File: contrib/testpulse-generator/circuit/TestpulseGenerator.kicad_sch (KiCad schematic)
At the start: 10 parts, among them Q1 STP16NF06, SW1 SW_DIP_x01, U1 Pico

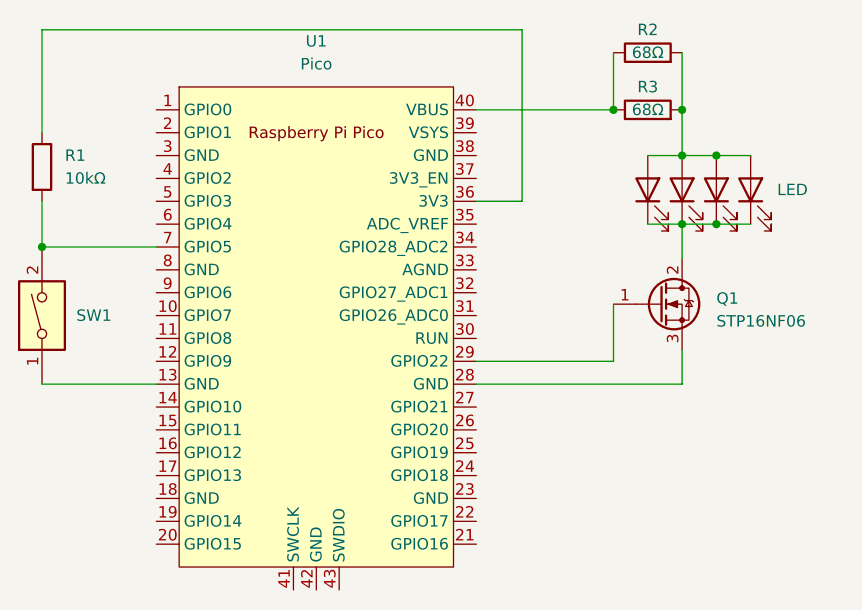
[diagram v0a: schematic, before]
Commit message: testpulse-generator: Drive TTL out separately
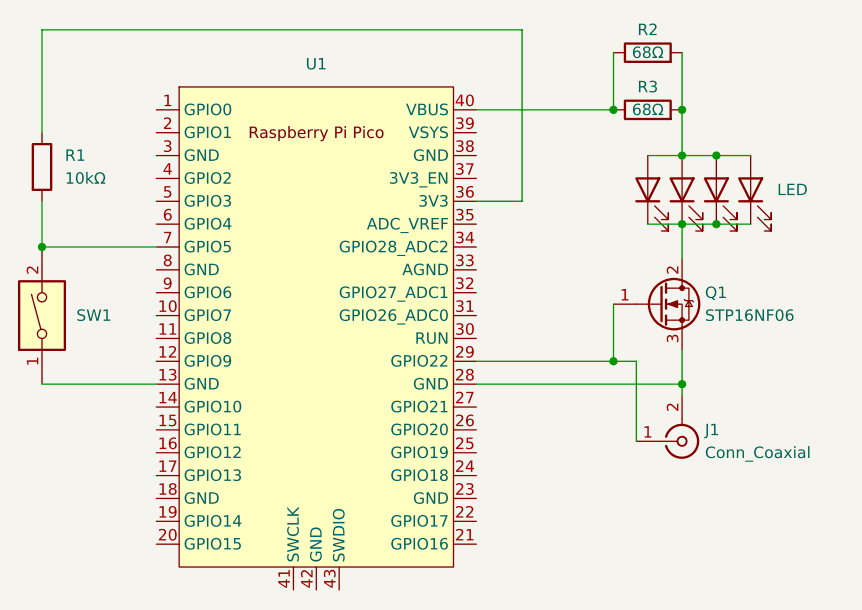
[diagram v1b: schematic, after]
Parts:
- added J1: Conn_Coaxial, symbol Connector:Conn_Coaxial
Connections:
- net at Q1.3 (S), U1.28 (GND): now also J1.2 (Ext)
- net at Q1.1 (G), U1.29 (GPIO22): now also J1.1 (In)
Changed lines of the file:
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@@
   (junction (at 106.68 52.07) (diameter 0) (color 0 0 0 0)
   )
+  (junction (at 99.06 67.31) (diameter 0) (color 0 0 0 0)
+  )
   (junction (at 99.06 39.37) (diameter 0) (color 0 0 0 0)
   )
   (junction (at 106.68 39.37) (diameter 0) (color 0 0 0 0)
   )
+  (junction (at 106.68 69.85) (diameter 0) (color 0 0 0 0)
+  )
   (junction (at 106.68 44.45) (diameter 0) (color 0 0 0 0)
   )
@@
     (stroke (width 0) (type default))
   )
+  (wire (pts (xy 101.6 67.31) (xy 99.06 67.31))
+    (stroke (width 0) (type default))
+  )
   (wire (pts (xy 110.49 44.45) (xy 114.3 44.45))
     (stroke (width 0) (type default))
@@
     (stroke (width 0) (type default))
   )
+  (wire (pts (xy 106.68 69.85) (xy 106.68 71.12))
+    (stroke (width 0) (type default))
+  )
   (wire (pts (xy 106.68 52.07) (xy 110.49 52.07))
+    (stroke (width 0) (type default))
+  )
+  (wire (pts (xy 101.6 76.2) (xy 101.6 67.31))
     (stroke (width 0) (type default))
   )
@@
   )
   (symbol (lib_id "Device:R") (at 35.56 45.72 0) (unit 1)
-    (in_bom yes) (on_board yes) (dnp no) (fields_autoplaced)
-    (property "Reference" "R1" (at 38.1 44.4499 0)
-      (effects (font (size 1.27 1.27)) (justify left))
-    )
-    (property "Value" "10kΩ" (at 38.1 46.9899 0)
+    (in_bom yes) (on_board yes) (dnp no)
+    (property "Reference" "R1" (at 38.1 44.45 0)
+      (effects (font (size 1.27 1.27)) (justify left))
+    )
+    (property "Value" "10kΩ" (at 38.1 46.99 0)
       (effects (font (size 1.27 1.27)) (justify left))
     )
@@
   )
   (symbol (lib_id "MCU_RaspberryPi_and_Boards:Pico") (at 66.04 63.5 0) (unit 1)
-    (in_bom yes) (on_board yes) (dnp no) (fields_autoplaced)
-    (property "Reference" "U1" (at 66.04 31.75 0)
-      (effects (font (size 1.27 1.27)))
-    )
-    (property "Value" "Pico" (at 66.04 34.29 0)
-      (effects (font (size 1.27 1.27)))
+    (in_bom yes) (on_board yes) (dnp no)
+    (property "Reference" "U1" (at 66.04 34.29 0)
+      (effects (font (size 1.27 1.27)))
+    )
+    (property "Value" "Pico" (at 66.04 35.56 0)
+      (effects (font (size 1.27 1.27)) hide)
     )
     (property "Footprint" "RPi_Pico:RPi_Pico_SMD_TH" (at 66.04 63.5 90)
@@
   )
   (symbol (lib_id "Transistor_FET:IRLZ24") (at 104.14 60.96 0) (unit 1)
-    (in_bom yes) (on_board yes) (dnp no) (fields_autoplaced)
-    (property "Reference" "Q1" (at 110.49 60.325 0)
-      (effects (font (size 1.27 1.27)) (justify left))
-    )
-    (property "Value" "STP16NF06 " (at 110.49 62.865 0)
+    (in_bom yes) (on_board yes) (dnp no)
+    (property "Reference" "Q1" (at 109.22 59.69 0)
+      (effects (font (size 1.27 1.27)) (justify left))
+    )
+    (property "Value" "STP16NF06 " (at 109.22 62.23 0)
       (effects (font (size 1.27 1.27)) (justify left))
     )
@@
         )
       )
+    )
+  )
+  (symbol (lib_id "Connector:Conn_Coaxial") (at 106.68 76.2 0) (mirror x) (unit 1)
+    (in_bom yes) (on_board yes) (dnp no)
+    (property "Reference" "J1" (at 109.22 74.93 0)
+      (effects (font (size 1.27 1.27)) (justify left))
+    )
+    (property "Value" "Conn_Coaxial" (at 109.22 77.47 0)
+      (effects (font (size 1.27 1.27)) (justify left))
+    )
+    (property "Footprint" "" (at 106.68 76.2 0)
+      (effects (font (size 1.27 1.27)) hide)
+    )
+    (property "Datasheet" " ~" (at 106.68 76.2 0)
+      (effects (font (size 1.27 1.27)) hide)
+    )
+    (pin "1")
+    (pin "2")
+    (instances
+      (project "TestpulseGenerator"
+        (path "/92024667-81f2-4122-830a-874e8ce8948c"
+          (reference "J1") (unit 1)
+        )
+      )
